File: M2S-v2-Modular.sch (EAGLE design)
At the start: 75 parts, among them J5 Qwiic Right Angle, J6 SM05B-SRSS-TB, U1 INA333AIDGKT, U2 LMV324, U3 INA333AIDGKT, U4 INA333AIDGKT, U5 INA333AIDGKT, U6 REF2033AIDDCT, U7 ADS1115IDGST

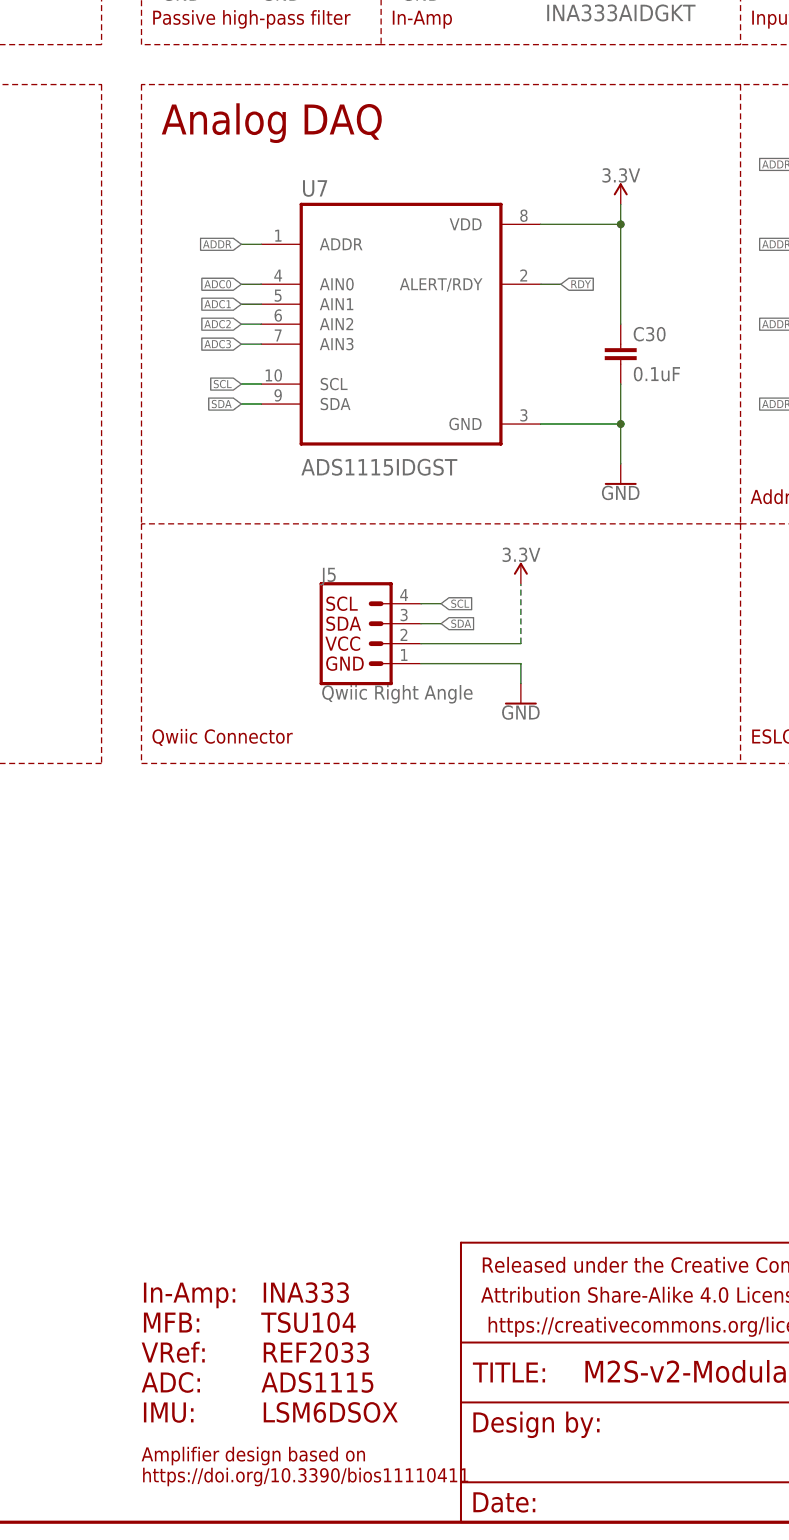
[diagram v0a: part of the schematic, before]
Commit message: ADC Fix
Changed ADC from ADS1115 to ADS1015.

Added EAGLE libraries.

Updated/Fixed JLCPCB BOM and PnP files.

Added PDF for the schematics for easier access.
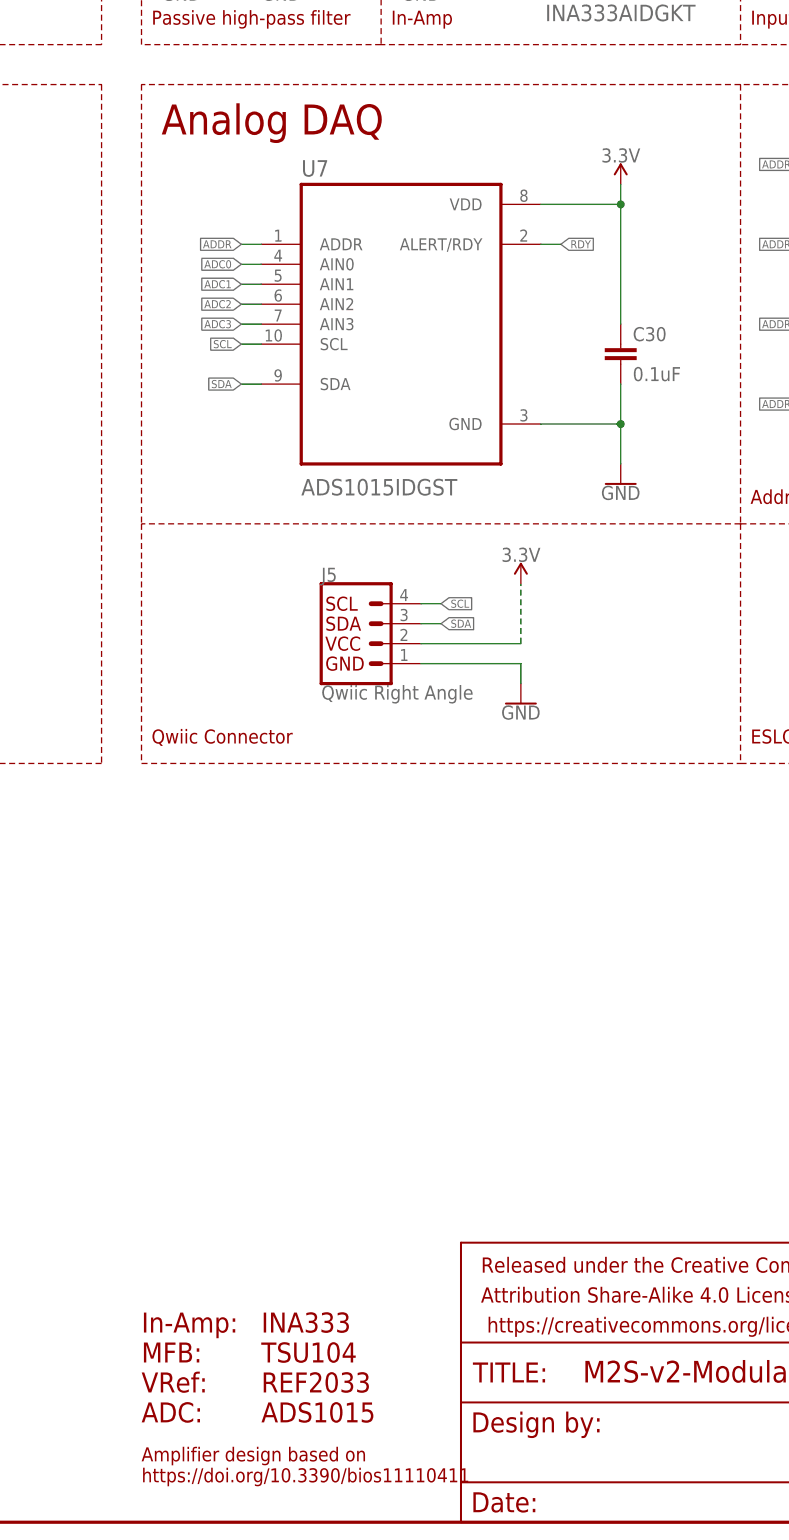
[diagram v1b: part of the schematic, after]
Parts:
- U7: value ADS1115IDGST -> ADS1015IDGST; device ADS1115IDGST:ADS1115IDGST -> ADS1015IDGST:ADS1015IDGST
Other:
- note added: "INA333 TSU104 REF2033 ADS1015"
- note added: "In-Amp: MFB: VRef: ADC:"
- note removed: "INA333 TSU104 REF2033 ADS1115 LSM6DSOX"
- note removed: "In-Amp: MFB: VRef: ADC: IMU:"
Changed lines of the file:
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@@
 <part name="GND22" library="SparkFun-PowerSymbols" library_urn="urn:adsk.eagle:library:530" deviceset="GND" device=""/>
 <part name="GND23" library="SparkFun-PowerSymbols" library_urn="urn:adsk.eagle:library:530" deviceset="GND" device=""/>
-<part name="U7" library="ADS1115IDGST" deviceset="ADS1115IDGST" device=""/>
 <part name="C30" library="SparkFun-Capacitors" library_urn="urn:adsk.eagle:library:510" deviceset="0.1UF" device="-0402-6.3V-10%-X7R" package3d_urn="urn:adsk.eagle:package:41385089/1" value="0.1uF"/>
 <part name="SUPPLY34" library="SparkFun-PowerSymbols" library_urn="urn:adsk.eagle:library:530" deviceset="3.3V" device=""/>
@@
 <part name="R30" library="SparkFun-Resistors" library_urn="urn:adsk.eagle:library:532" deviceset="10KOHM" device="-0402-1/16W-1%" package3d_urn="urn:adsk.eagle:package:39657/2" value="10k"/>
 <part name="R31" library="SparkFun-Resistors" library_urn="urn:adsk.eagle:library:532" deviceset="10KOHM" device="-0402-1/16W-1%" package3d_urn="urn:adsk.eagle:package:39657/2" value="10k"/>
+<part name="U7" library="ADS1015IDGST" deviceset="ADS1015IDGST" device=""/>
 </parts>
 <sheets>
@@
 MFB:
 VRef:
-ADC:
-IMU:</text>
+ADC:</text>
 <text x="304.8" y="12.7" size="2.54" layer="94" font="vector">INA333
 TSU104
 REF2033
-ADS1115
-LSM6DSOX</text>
+ADS1015</text>
 <text x="289.56" y="5.08" size="1.778" layer="94">Amplifier design based on
 https://doi.org/10.3390/bios11110411</text>
@@
 <attribute name="VALUE" x="259.08" y="126.746" size="1.778" layer="96" font="vector" align="top-center"/>
 </instance>
-<instance part="U7" gate="A" x="322.58" y="152.4" smashed="yes">
-<attribute name="NAME" x="309.88" y="168.64" size="2.0828" layer="95" ratio="10" rot="SR0"/>
-<attribute name="VALUE" x="309.88" y="133.16" size="2.0828" layer="96" ratio="10" rot="SR0"/>
-</instance>
 <instance part="C30" gate="G$1" x="350.52" y="147.32" smashed="yes">
 <attribute name="NAME" x="352.044" y="150.241" size="1.778" layer="95" font="vector"/>
 <attribute name="VALUE" x="352.044" y="145.161" size="1.778" layer="96" font="vector"/>
 </instance>
-<instance part="SUPPLY34" gate="G$1" x="350.52" y="167.64" smashed="yes">
-<attribute name="VALUE" x="350.52" y="170.434" size="1.778" layer="96" font="vector" align="bottom-center"/>
+<instance part="SUPPLY34" gate="G$1" x="350.52" y="170.18" smashed="yes">
+<attribute name="VALUE" x="350.52" y="172.974" size="1.778" layer="96" font="vector" align="bottom-center"/>
 </instance>
 <instance part="GND24" gate="1" x="350.52" y="132.08" smashed="yes">
@@
 <attribute name="NAME" x="411.48" y="148.844" size="1.778" layer="95" font="vector" align="bottom-center"/>
 <attribute name="VALUE" x="411.48" y="145.796" size="1.778" layer="96" font="vector" align="top-center"/>
+</instance>
+<instance part="U7" gate="A" x="322.58" y="152.4" smashed="yes">
+<attribute name="NAME" x="309.88" y="171.18" size="2.0828" layer="95" ratio="10" rot="SR0"/>
+<attribute name="VALUE" x="309.88" y="130.62" size="2.0828" layer="96" ratio="10" rot="SR0"/>
 </instance>
 </instances>
@@
 <segment>
 <pinref part="GND24" gate="1" pin="GND"/>
-<pinref part="U7" gate="A" pin="GND"/>
 <wire x1="350.52" y1="134.62" x2="350.52" y2="139.7" width="0.1524" layer="91"/>
 <wire x1="350.52" y1="139.7" x2="340.36" y2="139.7" width="0.1524" layer="91"/>
@@
 <wire x1="350.52" y1="144.78" x2="350.52" y2="139.7" width="0.1524" layer="91"/>
 <junction x="350.52" y="139.7"/>
+<pinref part="U7" gate="A" pin="GND"/>
 </segment>
 <segment>
@@
 </segment>
 <segment>
+<wire x1="302.26" y1="160.02" x2="304.8" y2="160.02" width="0.1524" layer="91"/>
+<label x="302.26" y="160.02" size="1.016" layer="95" rot="R180" xref="yes"/>
 <pinref part="U7" gate="A" pin="AIN0"/>
-<wire x1="302.26" y1="157.48" x2="304.8" y2="157.48" width="0.1524" layer="91"/>
-<label x="302.26" y="157.48" size="1.016" layer="95" rot="R180" xref="yes"/>
 </segment>
 </net>
@@
 </segment>
 <segment>
+<wire x1="302.26" y1="157.48" x2="304.8" y2="157.48" width="0.1524" layer="91"/>
+<label x="302.26" y="157.48" size="1.016" layer="95" rot="R180" xref="yes"/>
 <pinref part="U7" gate="A" pin="AIN1"/>
-<wire x1="302.26" y1="154.94" x2="304.8" y2="154.94" width="0.1524" layer="91"/>
-<label x="302.26" y="154.94" size="1.016" layer="95" rot="R180" xref="yes"/>
 </segment>
 </net>
@@
 </segment>
 <segment>
+<wire x1="302.26" y1="154.94" x2="304.8" y2="154.94" width="0.1524" layer="91"/>
+<label x="302.26" y="154.94" size="1.016" layer="95" rot="R180" xref="yes"/>
 <pinref part="U7" gate="A" pin="AIN2"/>
-<wire x1="302.26" y1="152.4" x2="304.8" y2="152.4" width="0.1524" layer="91"/>
-<label x="302.26" y="152.4" size="1.016" layer="95" rot="R180" xref="yes"/>
 </segment>
 </net>
@@
 </segment>
 <segment>
+<wire x1="302.26" y1="152.4" x2="304.8" y2="152.4" width="0.1524" layer="91"/>
+<label x="302.26" y="152.4" size="1.016" layer="95" rot="R180" xref="yes"/>
 <pinref part="U7" gate="A" pin="AIN3"/>
-<wire x1="302.26" y1="149.86" x2="304.8" y2="149.86" width="0.1524" layer="91"/>
-<label x="302.26" y="149.86" size="1.016" layer="95" rot="R180" xref="yes"/>
 </segment>
 </net>
@@
 </segment>
 <segment>
+<pinref part="SUPPLY34" gate="G$1" pin="3.3V"/>
+<wire x1="340.36" y1="167.64" x2="350.52" y2="167.64" width="0.1524" layer="91"/>
+<wire x1="350.52" y1="167.64" x2="350.52" y2="170.18" width="0.1524" layer="91"/>
+<pinref part="C30" gate="G$1" pin="1"/>
+<wire x1="350.52" y1="167.64" x2="350.52" y2="152.4" width="0.1524" layer="91"/>
+<junction x="350.52" y="167.64"/>
 <pinref part="U7" gate="A" pin="VDD"/>
-<pinref part="SUPPLY34" gate="G$1" pin="3.3V"/>
-<wire x1="340.36" y1="165.1" x2="350.52" y2="165.1" width="0.1524" layer="91"/>
-<wire x1="350.52" y1="165.1" x2="350.52" y2="167.64" width="0.1524" layer="91"/>
-<pinref part="C30" gate="G$1" pin="1"/>
-<wire x1="350.52" y1="165.1" x2="350.52" y2="152.4" width="0.1524" layer="91"/>
-<junction x="350.52" y="165.1"/>
 </segment>
 <segment>
@@
 <net name="ADDR" class="0">
 <segment>
-<pinref part="U7" gate="A" pin="ADDR"/>
 <wire x1="302.26" y1="162.56" x2="304.8" y2="162.56" width="0.1524" layer="91"/>
 <label x="302.26" y="162.56" size="1.016" layer="95" rot="R180" xref="yes"/>
+<pinref part="U7" gate="A" pin="ADDR"/>
 </segment>
 <segment>
@@
 <net name="SCL" class="0">
 <segment>
+<wire x1="302.26" y1="149.86" x2="304.8" y2="149.86" width="0.1524" layer="91"/>
+<label x="302.26" y="149.86" size="1.016" layer="95" rot="R180" xref="yes"/>
 <pinref part="U7" gate="A" pin="SCL"/>
-<wire x1="302.26" y1="144.78" x2="304.8" y2="144.78" width="0.1524" layer="91"/>
-<label x="302.26" y="144.78" size="1.016" layer="95" rot="R180" xref="yes"/>
 </segment>
 <segment>
@@
 <net name="SDA" class="0">
 <segment>
+<wire x1="302.26" y1="144.78" x2="304.8" y2="144.78" width="0.1524" layer="91"/>
+<label x="302.26" y="144.78" size="1.016" layer="95" rot="R180" xref="yes"/>
 <pinref part="U7" gate="A" pin="SDA"/>
-<wire x1="302.26" y1="142.24" x2="304.8" y2="142.24" width="0.1524" layer="91"/>
-<label x="302.26" y="142.24" size="1.016" layer="95" rot="R180" xref="yes"/>
 </segment>
 <segment>
@@
 <net name="RDY" class="0">
 <segment>
+<wire x1="342.9" y1="162.56" x2="340.36" y2="162.56" width="0.1524" layer="91"/>
+<label x="342.9" y="162.56" size="1.016" layer="95" xref="yes"/>
 <pinref part="U7" gate="A" pin="ALERT/RDY"/>
-<wire x1="342.9" y1="157.48" x2="340.36" y2="157.48" width="0.1524" layer="91"/>
-<label x="342.9" y="157.48" size="1.016" layer="95" xref="yes"/>
-</segment>
-<segment>
+</segment>
+<segment>

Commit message: Fix ESLOV Pinout
Fixed ESLOV Pinout, swapped SDA and INT pins.
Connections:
- net RDY: now also J6-2.P; no longer J6-4.P
- net SDA: now also J6-4.P; no longer J6-2.P
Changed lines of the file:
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@@
 </segment>
 <segment>
-<pinref part="J6" gate="-2" pin="P"/>
-<wire x1="393.7" y1="116.84" x2="391.16" y2="116.84" width="0.1524" layer="91" style="longdash"/>
-<label x="393.7" y="116.84" size="1.016" layer="95" xref="yes"/>
+<pinref part="J6" gate="-4" pin="P"/>
+<wire x1="393.7" y1="111.76" x2="391.16" y2="111.76" width="0.1524" layer="91" style="longdash"/>
+<label x="393.7" y="111.76" size="1.016" layer="95" xref="yes"/>
 </segment>
 </net>
@@
 </segment>
 <segment>
-<pinref part="J6" gate="-4" pin="P"/>
-<wire x1="393.7" y1="111.76" x2="391.16" y2="111.76" width="0.1524" layer="91" style="longdash"/>
-<label x="393.7" y="111.76" size="1.016" layer="95" xref="yes"/>
+<pinref part="J6" gate="-2" pin="P"/>
+<wire x1="393.7" y1="116.84" x2="391.16" y2="116.84" width="0.1524" layer="91" style="longdash"/>
+<label x="393.7" y="116.84" size="1.016" layer="95" xref="yes"/>
 </segment>
 </net>
